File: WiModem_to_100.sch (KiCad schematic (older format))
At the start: 2 parts, among them J1 DB25_Male, J2 DB25_Male

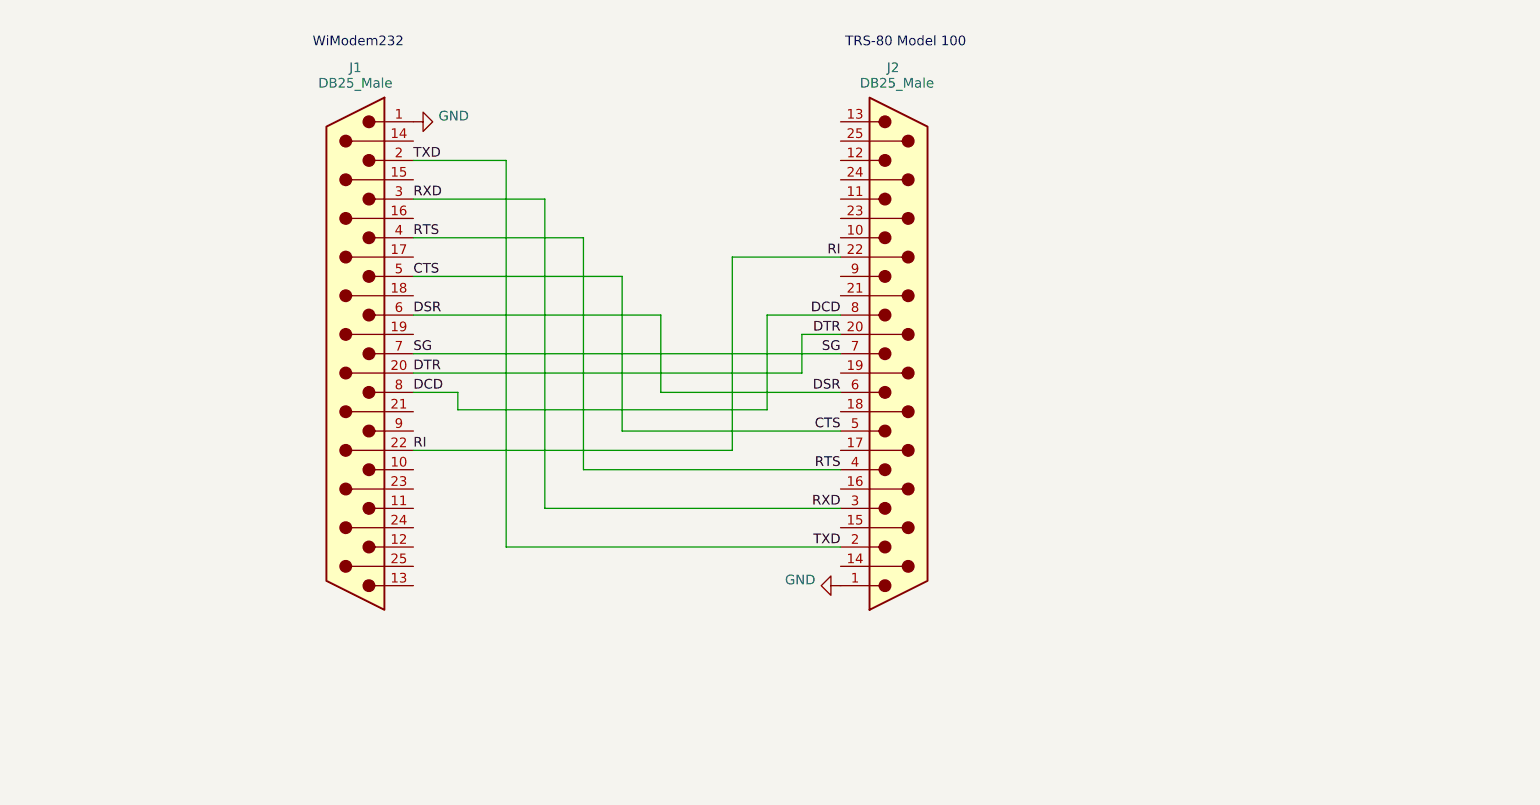
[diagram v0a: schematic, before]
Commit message: notes in .sch, remove .stl, change img from png to jpg
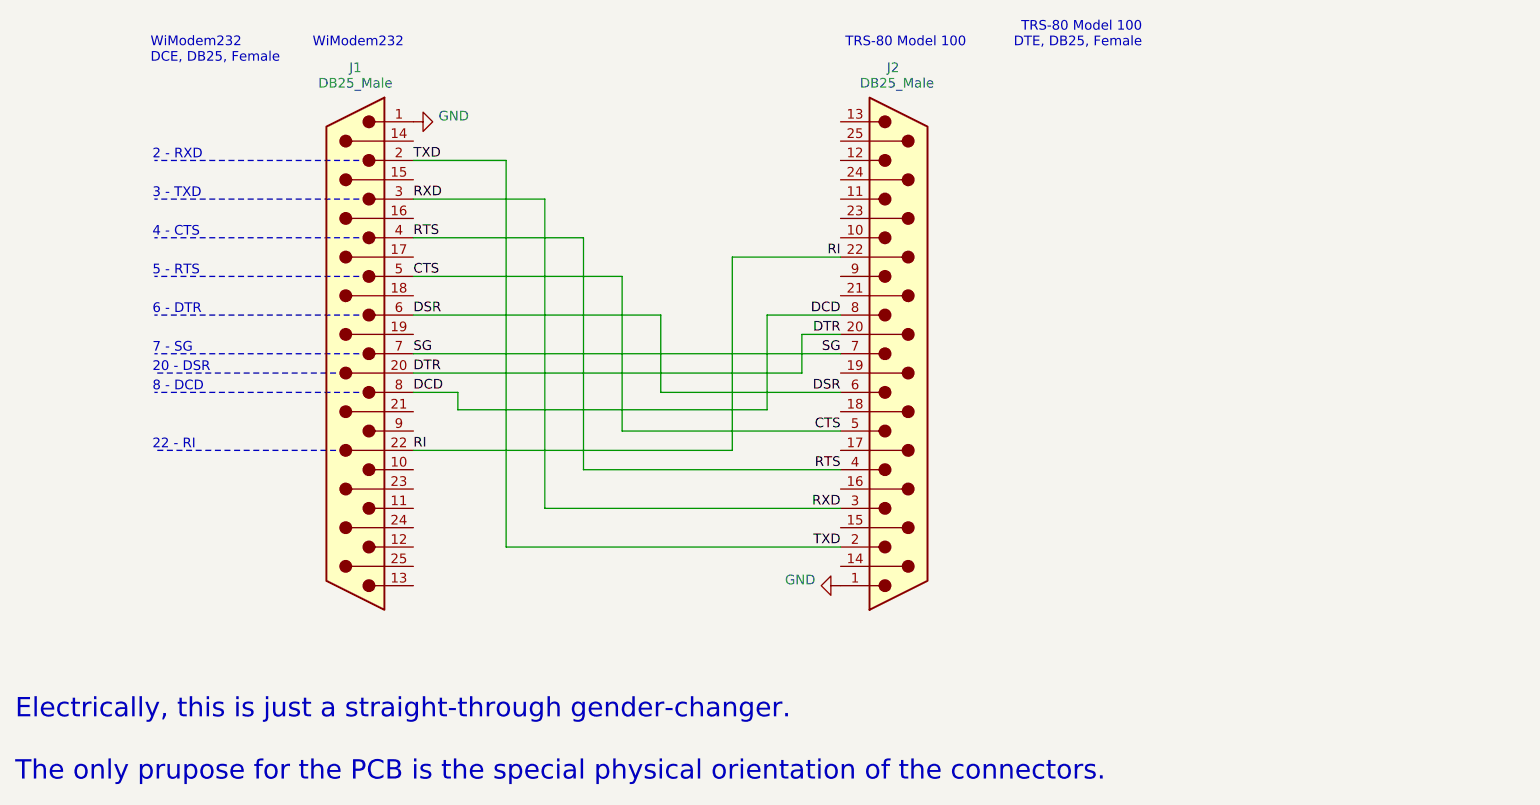
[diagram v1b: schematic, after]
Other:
- note added: "2 - RXD"
- note added: "20 - DSR"
- note added: "22 - RI"
- note added: "3 - TXD"
- note added: "4 - CTS"
- note added: "5 - RTS"
- note added: "6 - DTR"
- note added: "7 - SG"
- note added: "8 - DCD"
- note added: "Electrically, this is just a straight-through gender-changer.\n\nThe only prupose for the PCB is the special physical orientation of the connectors."
- note added: "TRS-80 Model 100\nDTE, DB25, Female"
- note added: "WiModem232\nDCE, DB25, Female"
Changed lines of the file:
@@
 	0    -1   -1   0
 $EndComp
+Text Notes 3060 2500 0    50   ~ 0
+WiModem232\nDCE, DB25, Female
+Text Notes 3070 3000 0    50   ~ 0
+2 - RXD
+Wire Notes Line
+	4140 3000 3080 3000
+Text Notes 3070 3200 0    50   ~ 0
+3 - TXD
+Wire Notes Line
+	4140 3200 3080 3200
+Text Notes 3070 3400 0    50   ~ 0
+4 - CTS
+Wire Notes Line
+	4140 3400 3080 3400
+Text Notes 3070 3600 0    50   ~ 0
+5 - RTS
+Wire Notes Line
+	4140 3600 3080 3600
+Text Notes 3070 3800 0    50   ~ 0
+6 - DTR
+Wire Notes Line
+	4140 3800 3080 3800
+Text Notes 3070 4000 0    50   ~ 0
+7 - SG
+Wire Notes Line
+	4140 4000 3080 4000
+Text Notes 3070 4100 0    50   ~ 0
+20 - DSR
+Text Notes 3070 4500 0    50   ~ 0
+22 - RI
+Text Notes 3070 4200 0    50   ~ 0
+8 - DCD
+Wire Notes Line
+	4140 4200 3080 4200
+Wire Notes Line
+	4020 4100 3080 4100
+Wire Notes Line
+	4020 4500 3080 4500
+Text Notes 8190 2420 2    50   ~ 0
+TRS-80 Model 100\nDTE, DB25, Female
+Text Notes 2360 6220 0    100  ~ 0
+Electrically, this is just a straight-through gender-changer.\n\nThe only prupose for the PCB is the special physical orientation of the connectors.
 $EndSCHEMATC
